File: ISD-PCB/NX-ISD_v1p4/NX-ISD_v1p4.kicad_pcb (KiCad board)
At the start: 4 copper layers, 77 x 48.6 mm, 110 parts, among them J1 UJ20-C-H-G-SMT-1-P16-TR, J2 1-2328702-0, P1 S2B-PH-SM4-TB, Q1 BC847W, Q2 AO3401A, Q3 AO3400A, Q4 AO3400A, U1 RT9193-18GB, U10 OPT3001DNPR, U11 BNO085, U12 RV-3028-C7, U13 ESP32-S3-WROOM-1-N16R8, U14 ZDSD02GLGEAG, U16 TM-2025A, U2 USBLC6-2P6, U3 TLV62568DBV, U5 BQ25170DSGR, U6 MAX17048G_T10, U7 BME690, U8 MAX30102, U9 PCA9306, Y1 32.768 kHz

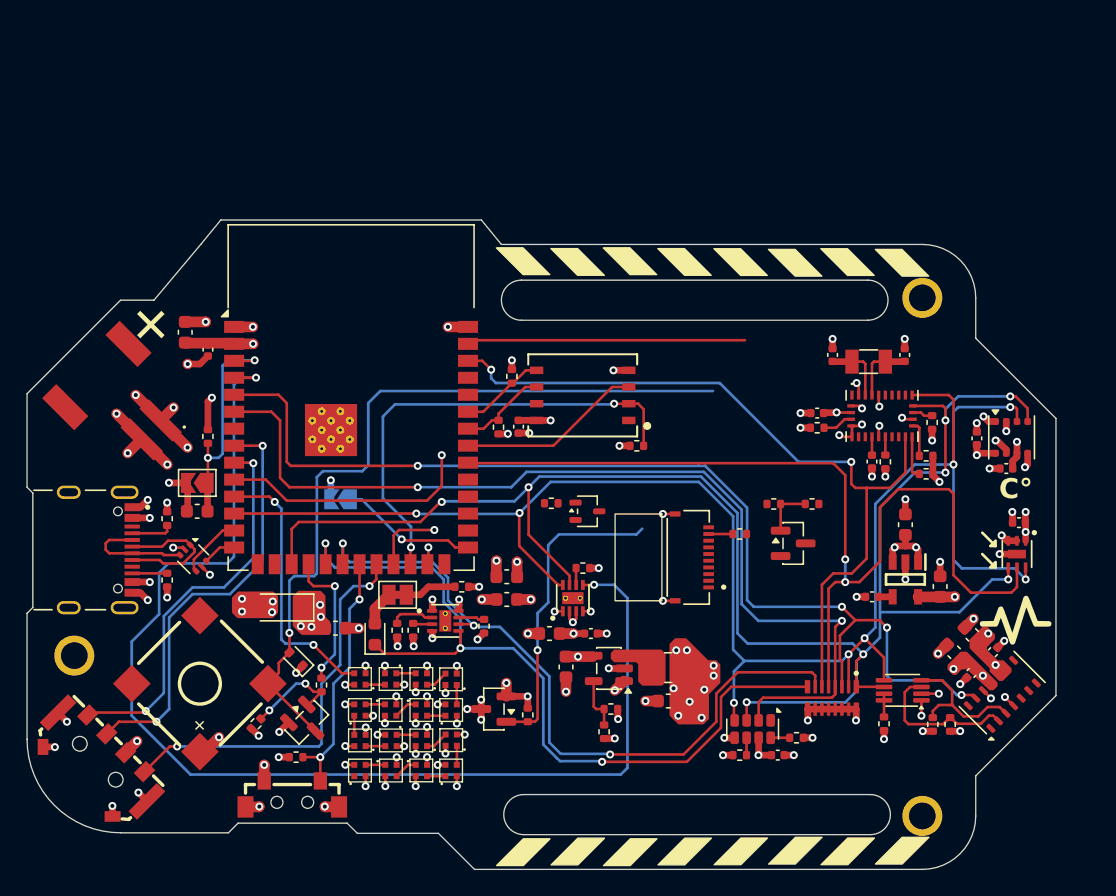
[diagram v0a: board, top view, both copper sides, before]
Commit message: feat(pcb): v1.4 schematic and layout updates for 4-bit SDMMC, direct display SPI, and button pullups
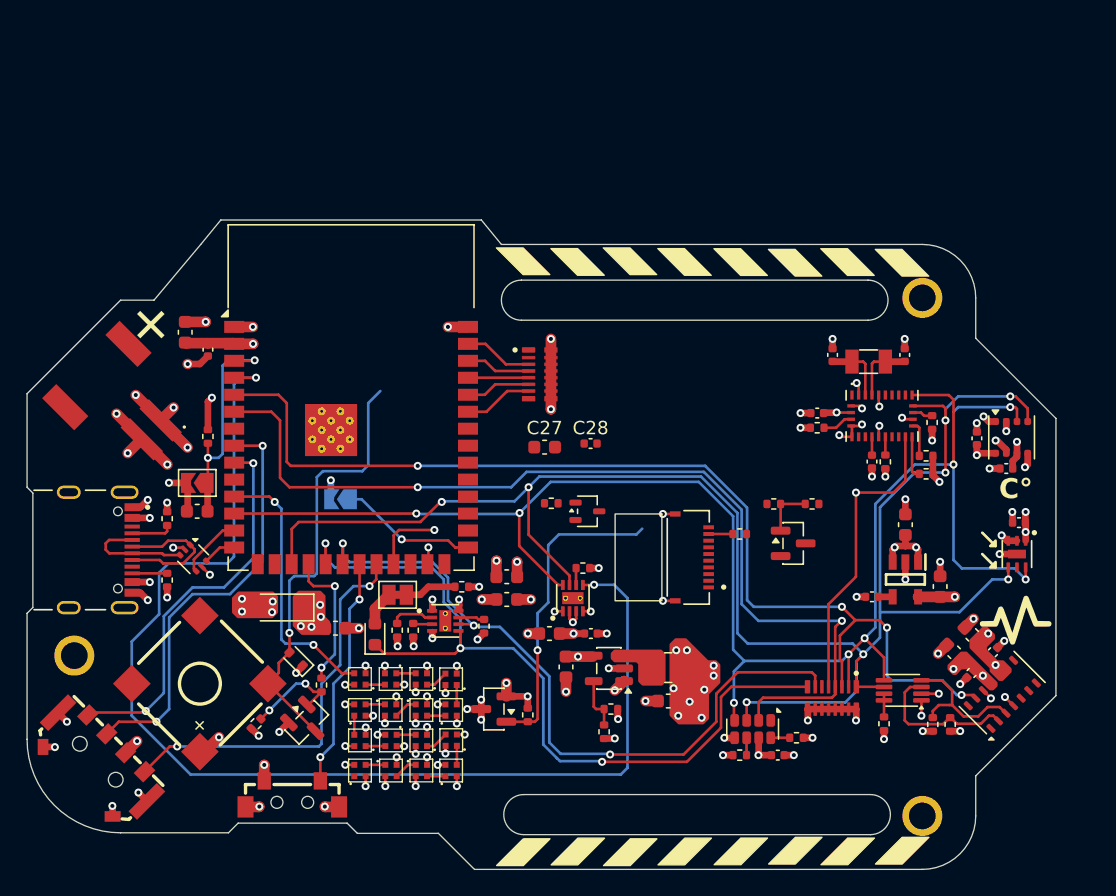
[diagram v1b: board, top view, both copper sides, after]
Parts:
- removed R20, R21, R22: 51.1k, Resistor_SMD:R_0402_1005Metric
- removed R30: 10k, Resistor_SMD:R_0402_1005Metric
- removed U14: ZDSD02GLGEAG, NX-AW-footprints:LGA-8_L8.0-W6.0-P1.27-TL_ZDSD02GLGEAG
- added C28: 100n, Capacitor_SMD:C_0402_1005Metric, F.Cu at (154.5, 94.8)
- added RN2: YC248-JR-074K7L, NX-AW-footprints:RESCAXS50P400X160X55-16N, F.Cu at (150.7, 89.7)
- C27: value 100n -> 10u; footprint Capacitor_SMD:C_0402_1005Metric -> Capacitor_SMD:C_0603_1608Metric
- moved C27 2.48 mm to (151.1, 95.1), turned to 0 degrees
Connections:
- RN1 pad 5: /Logic section/!INT_ALS -> /Logic section/!INT_DOF
- RN1 pad 6: /Logic section/!INT_H -> /Logic section/!ALERT
- RN1 pad 7: /Logic section/USB_DETECT -> /Logic section/BAT_STAT
- RN1 pad 8: /Logic section/BAT_STAT -> /Logic section/USB_DETECT
- U10 pad 5: /Logic section/!INT_ALS -> unconnected-(U10-INT-Pad5)
- U11 pad 14: /Logic section/!INT_H -> /Logic section/!INT_DOF
- U13 pad 24: /Logic section/CS_SD -> /Logic section/PWM_TFT
- U13 pad 32: /Logic section/!INT_ALS -> /Logic section/SCK
- U13 pad 33: /Logic section/SCK -> /Logic section/MOSI
- U13 pad 34: /Logic section/MISO -> /Logic section/SD_CLK
- U13 pad 35: /Logic section/MOSI -> /Logic section/SD_DAT2
- U13 pad 36: unconnected-(U13-RXD0-Pad36) -> /Logic section/SD_DAT1
- U13 pad 37: unconnected-(U13-TXD0-Pad37) -> /Logic section/SD_DAT0
- U13 pad 38: /Logic section/!INT_H -> /Logic section/CS_SD
- U13 pad 39: /Logic section/PWM_TFT -> /Logic section/SD_CMD
- U13 pad 7: unconnected-(U13-IO7-Pad7) -> /Logic section/!INT_DOF
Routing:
- net /Logic section/!INT_ALS: track 71.9 -> 0.00 mm, vias 2 -> 0
- net /Logic section/!INT_H: track 58.3 -> 0.00 mm, vias 2 -> 0
- net /Logic section/CS_SD: track 34.8 -> 4.85 mm, vias 2 -> 0
- net Net-(D3-A): track 57.9 -> 33.0 mm
- net /Logic section/!INT_DOF: track 0.00 -> 22.7 mm, vias 0 -> 1
- net /Logic section/PWM_TFT: track 20.8 -> 0.00 mm
- net /Logic section/PWR_NPM: track 18.9 -> 0.00 mm, vias 1 -> 0
- net /Logic section/SCK: track 13.9 -> 0.06 mm
- net /Logic section/MISO: track 6.71 -> 0.00 mm
- net /Logic section/MOSI: track 6.42 -> 0.00 mm
- net /Logic section/SD_DAT2: track 0.00 -> 5.18 mm
- net /Logic section/SD_CMD: track 0.00 -> 5.17 mm
- net /Logic section/SD_DAT1: track 0.00 -> 4.86 mm
- net /Logic section/SD_DAT0: track 0.00 -> 4.54 mm
- net GND: track 90.7 -> 88.7 mm, vias 93 -> 91
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
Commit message: hw(v1.4): relocate MicroSD to right edge and re-route BNO085 cluster; update READMEs
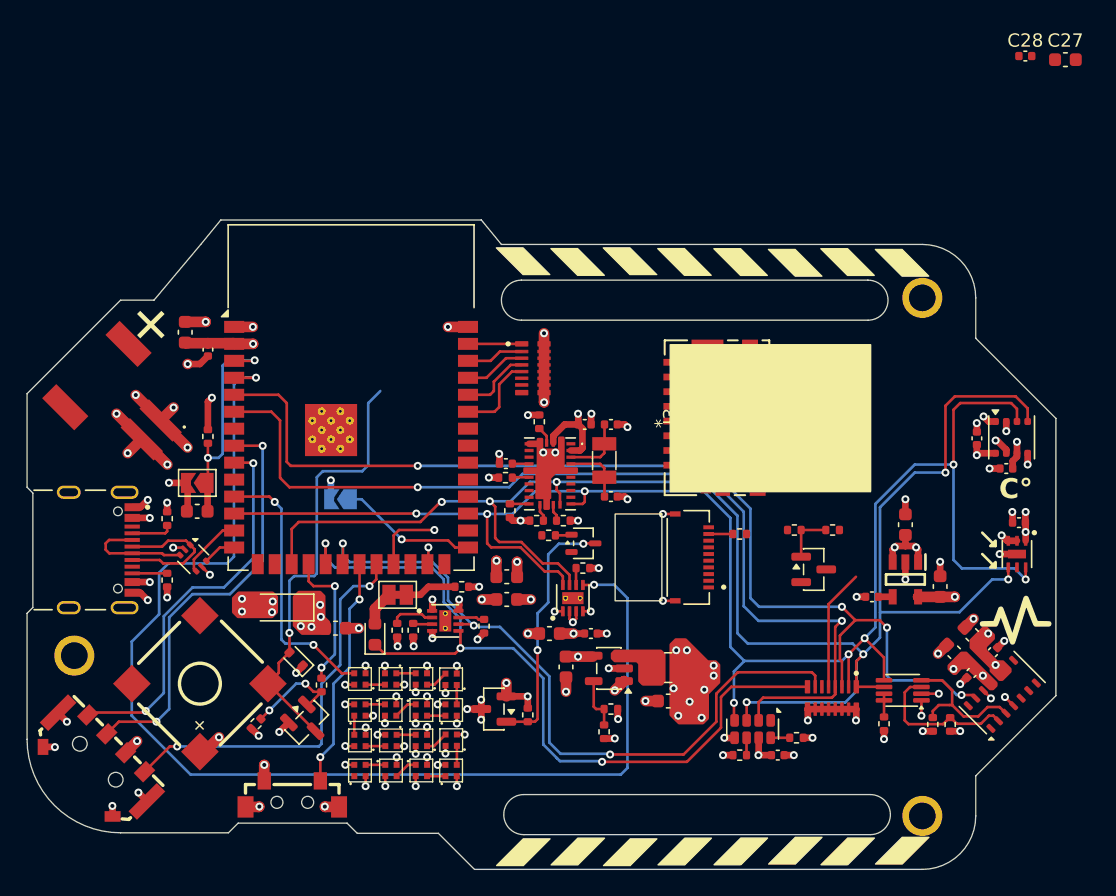
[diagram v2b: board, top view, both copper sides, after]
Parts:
- added J3: 1051620001, NX-AW-footprints:105162-0001_MOL, F.Cu at (164.0, 92.9)
- moved C27 48.6 mm to (190.1, 66.1)
- moved C28 43.6 mm to (187.1, 65.8)
- moved R17 31.3 mm to (148.5, 99.9), turned to 90 degrees
- moved R16 29.6 mm to (150.5, 100.6), turned to 0 degrees
- moved R14 28.6 mm to (152.5, 100.6), turned to 0 degrees
- moved R18 28.5 mm to (148.2, 97.4), turned to 0 degrees
- moved C21 27.4 mm to (148.2, 96.3), turned to 0 degrees
- moved U11 25.2 mm to (151.5, 97.1), turned to -90 degrees
- moved C23 24.4 mm to (156.1, 98.8), turned to 0 degrees
- moved Y1 21.1 mm to (155.6, 96.1), turned to 90 degrees
- moved R13 20.8 mm to (150.7, 93.2), turned to 90 degrees
- moved C19 17.4 mm to (154.1, 93.4), turned to 0 degrees
- moved C22 17.4 mm to (156.1, 93.4), turned to 0 degrees
- moved Q4 2.48 mm to (171.2, 104.2)
- moved R25 2.48 mm to (169.8, 101.3)
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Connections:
- RN2 pad 1: unconnected-(RN2-Pad1) -> /Logic section/SD_CMD
- RN2 pad 2: unconnected-(RN2-Pad2) -> /Logic section/CS_SD
- RN2 pad 3: /Logic section/SD_CMD -> /Logic section/SD_DAT0
- RN2 pad 4: /Logic section/CS_SD -> /Logic section/SD_DAT1
- RN2 pad 5: /Logic section/SD_DAT0 -> /Logic section/SD_DAT2
- RN2 pad 6: /Logic section/SD_DAT1 -> unconnected-(RN2-Pad6)
- RN2 pad 7: /Logic section/SD_DAT2 -> unconnected-(RN2-Pad7)
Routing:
- net /Logic section/!INT_DOF: track 22.7 -> 9.08 mm, vias 1 -> 0
- net GND: track 88.7 -> 83.4 mm, vias 91 -> 87
- net Net-(Q1-C): track 23.3 -> 18.9 mm, vias 1 -> 2
- net /Logic section/SDA_1: track 127.7 -> 123.7 mm
- net +3V3: track 44.2 -> 46.9 mm, vias 35 -> 34
- net Net-(U11-ENV_SCL): track 3.23 -> 1.44 mm
- net Net-(U11-ENV_SDA): track 2.64 -> 1.30 mm
- net Net-(Q1-B): track 0.00 -> 1.22 mm
- net /Logic section/SD_CMD: track 5.17 -> 4.02 mm
- net /Logic section/SD_DAT2: track 5.18 -> 6.26 mm
- net Net-(U11-~{BOOT}): track 2.29 -> 1.31 mm
- net /Logic section/CS_SD: track 4.85 -> 4.31 mm
- net /Logic section/SCL_1: track 129.4 -> 129.2 mm, vias 8 -> 7

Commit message: hw(v1.4): progress on TODO - 4-bit MicroSD, direct display bus, BNO085 & EP vias (DRC 0 errors)
- Implemented 4-bit SDMMC MicroSD slot (Molex 105162-0001) on right edge with outward insertion
- Routed direct 3.3V display SPI bus (TE 1-2328702-0) with C29 100nF decoupling
- Centered BNO085 9-DOF IMU cluster with local ground star and 32.768kHz crystal
- Rerouted NeoPixel PWR_NPM high-side power gate signal
- Updated thermal EP pad via sizes on BQ25170 and MAX17048 for standard JLCPCB fabrication
- Achieved 0 DRC errors, 0 unconnected nets, and 100% schematic parity
- Updated HW-TODO and SW-TODO for v1.3/v1.4 pinout target abstraction
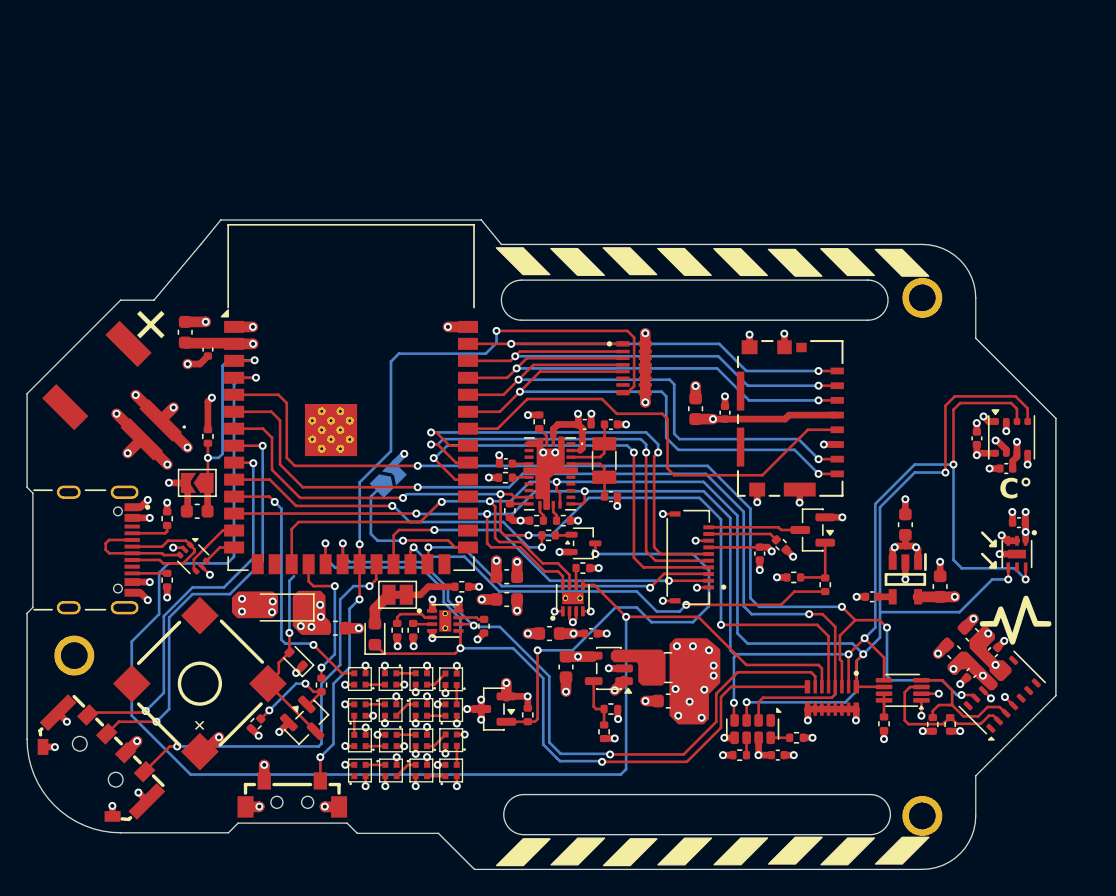
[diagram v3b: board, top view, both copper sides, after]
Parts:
- added C29: 100n, Capacitor_SMD:C_0402_1005Metric, F.Cu at (167.2, 103.1)
- moved C27 38.1 mm to (162.4, 92.2), turned to 90 degrees
- moved C28 34.9 mm to (164.6, 92.5), turned to 90 degrees
- moved RN2 7.58 mm to (157.8, 89.2)
- moved J3 5.48 mm to (169.5, 93.0), turned to 90 degrees
- moved R25 4.71 mm to (172.1, 105.4), turned to -90 degrees
- moved R26 4.59 mm to (169.7, 104.8), turned to 180 degrees
- moved JP3 3.88 mm to (139.4, 97.5), turned to 45 degrees
- moved R27 3.20 mm to (168.8, 102.4), turned to 135 degrees
- moved Q4 2.95 mm to (171.2, 101.3), turned to 180 degrees
- renumbered U16 to S2
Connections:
- J3 pad G1: unconnected-(J3-GND_2-PadG1) -> GND
- J3 pad G2: unconnected-(J3-GND_3-PadG2) -> GND
- J3 pad G3: unconnected-(J3-GND_4-PadG3) -> GND
- J3 pad G4: unconnected-(J3-GND-PadG4) -> GND
- J3 pad P1: unconnected-(J3-DAT2-PadP1) -> /Logic section/SD_DAT2
- J3 pad P2: unconnected-(J3-CD/DAT3-PadP2) -> /Logic section/CS_SD
- J3 pad P3: unconnected-(J3-CMD-PadP3) -> /Logic section/SD_CMD
- J3 pad P4: unconnected-(J3-VDD-PadP4) -> +3V3
- J3 pad P5: unconnected-(J3-CLK-PadP5) -> /Logic section/SD_CLK
- J3 pad P6: unconnected-(J3-VSS-PadP6) -> GND
- J3 pad P7: unconnected-(J3-DAT0-PadP7) -> /Logic section/SD_DAT0
- J3 pad P8: unconnected-(J3-DAT1-PadP8) -> /Logic section/SD_DAT1
- RN1 pad 7: /Logic section/BAT_STAT -> /Logic section/USB_DETECT
- RN1 pad 8: /Logic section/USB_DETECT -> /Logic section/BAT_STAT
- RN2 pad 1: /Logic section/SD_CMD -> /Logic section/SD_DAT2
- RN2 pad 3: /Logic section/SD_DAT0 -> /Logic section/SD_CMD
- RN2 pad 4: /Logic section/SD_DAT1 -> /Logic section/SD_DAT0
- RN2 pad 5: /Logic section/SD_DAT2 -> /Logic section/SD_DAT1
- U13 pad 31: /Logic section/RST -> /Logic section/SCK
- U13 pad 32: /Logic section/SCK -> /Logic section/MOSI
- U13 pad 33: /Logic section/MOSI -> /Logic section/RST
- U13 pad 35: /Logic section/SD_DAT2 -> /Logic section/SD_DAT1
- U13 pad 36: /Logic section/SD_DAT1 -> /Logic section/SD_DAT0
- U13 pad 37: /Logic section/SD_DAT0 -> /Logic section/SD_CMD
- U13 pad 39: /Logic section/SD_CMD -> /Logic section/SD_DAT2
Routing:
- net /Logic section/!INT_DOF: track 9.08 -> 67.2 mm, vias 0 -> 4
- net /Logic section/BTN: track 17.5 -> 58.1 mm, vias 2 -> 4
- net /Logic section/SD_DAT0: track 4.64 -> 41.0 mm, vias 0 -> 2
- net /Logic section/SD_DAT1: track 5.36 -> 41.0 mm, vias 0 -> 2
- net /Logic section/PWM_TFT: track 0.00 -> 34.8 mm, vias 0 -> 2
- net /Logic section/SD_CLK: track 0.00 -> 34.5 mm
- net /Logic section/SD_CMD: track 4.02 -> 37.2 mm, vias 0 -> 2
- net /Logic section/MOSI: track 0.00 -> 33.0 mm, vias 0 -> 2
- net /Logic section/RST: track 0.00 -> 32.7 mm, vias 0 -> 2
- net /Logic section/CS_SD: track 4.31 -> 36.9 mm, vias 0 -> 2
- net /Logic section/SCK: track 0.06 -> 32.6 mm, vias 0 -> 2
- net /Logic section/SD_DAT2: track 6.26 -> 36.8 mm, vias 0 -> 2
- net /Logic section/PWR_NPM: track 0.00 -> 26.0 mm, vias 0 -> 2
- net /Logic section/CS_TFT: track 1.50 -> 24.2 mm, vias 1 -> 2
- net /Logic section/DC: track 5.38 -> 27.5 mm, vias 1 -> 2
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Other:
- board text added: "SD-CARD"

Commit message: hw(v1.4): bq25170 thermal optimization, usb-c plating, battery pad stitching, and npm decoupling
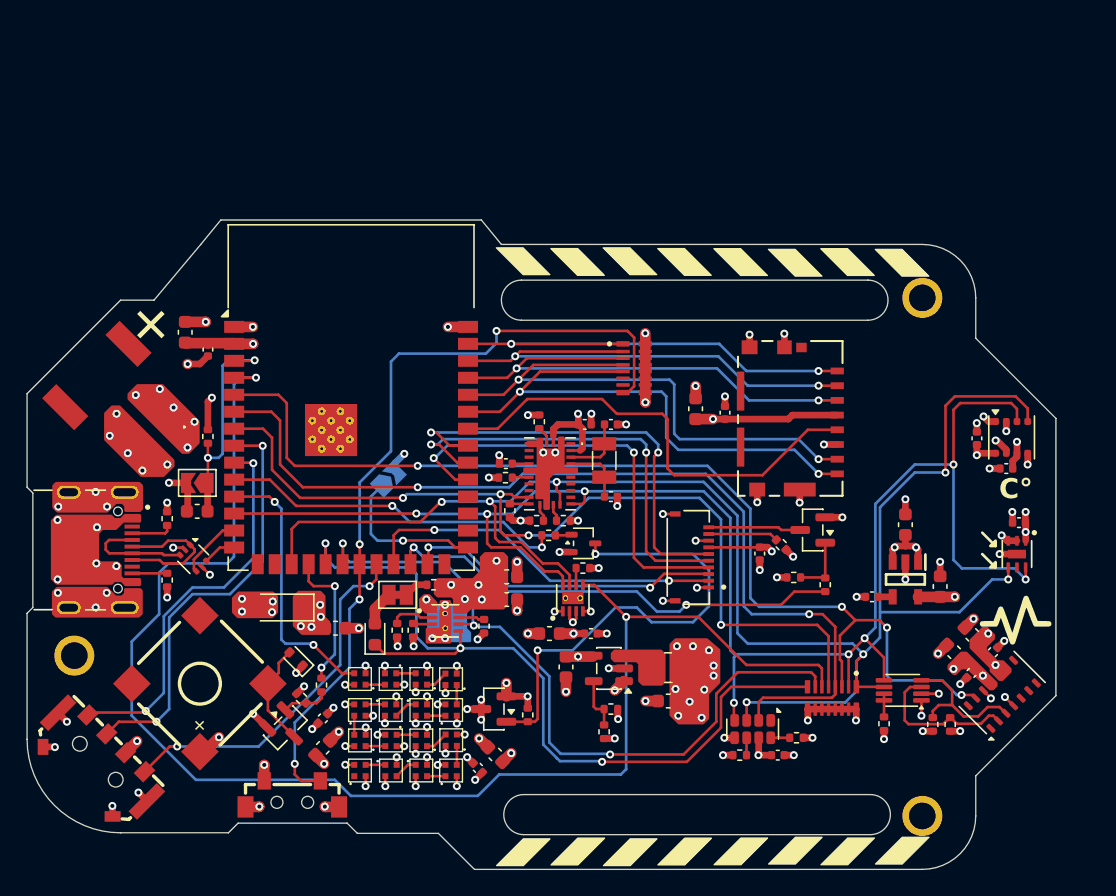
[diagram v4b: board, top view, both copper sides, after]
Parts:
- added C34: 100n, Capacitor_SMD:C_0402_1005Metric, F.Cu at (146.1, 119.1)
- added C35: 4.7u, Capacitor_SMD:C_0603_1608Metric, F.Cu at (147.4, 118.1)
- added C36: 100n, Capacitor_SMD:C_0402_1005Metric, F.Cu at (134.5, 115.4)
- added C37: 4.7u, Capacitor_SMD:C_0603_1608Metric, F.Cu at (134.5, 117.6)
- R6: value 499 -> 604
- moved R24 3.89 mm to (132.9, 113.9), turned to 135 degrees
- moved R9 2.11 mm to (142.8, 105.4)
- moved Q3 1.65 mm to (131.7, 116.1)
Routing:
- net VBAT: track 20.9 -> 12.5 mm, vias 13 -> 16
- net GND: track 95.2 -> 88.9 mm, vias 100 -> 112
- net Net-(D3-A): track 13.9 -> 7.80 mm, vias 1 -> 0
- net Net-(Q3-G): track 7.49 -> 3.55 mm, vias 2 -> 0
- net VN: track 12.3 -> 15.4 mm, vias 19 -> 23
- net /Power section/USB_P: track 3.48 -> 0.84 mm, vias 7 -> 10
- net /Logic section/LEVER_LEFT: track 30.0 -> 27.3 mm
- net /Logic section/BTN: track 58.1 -> 60.6 mm
- net Net-(JP1-A): track 3.89 -> 1.85 mm
- net /Logic section/!ALERT: track 106.3 -> 107.6 mm
- net /Logic section/BAT_STAT: track 61.6 -> 62.5 mm
- net /Logic section/USB_DETECT: track 53.3 -> 54.2 mm
- net VBUS: track 0.78 -> 0.03 mm
